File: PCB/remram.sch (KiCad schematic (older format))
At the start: 0 parts

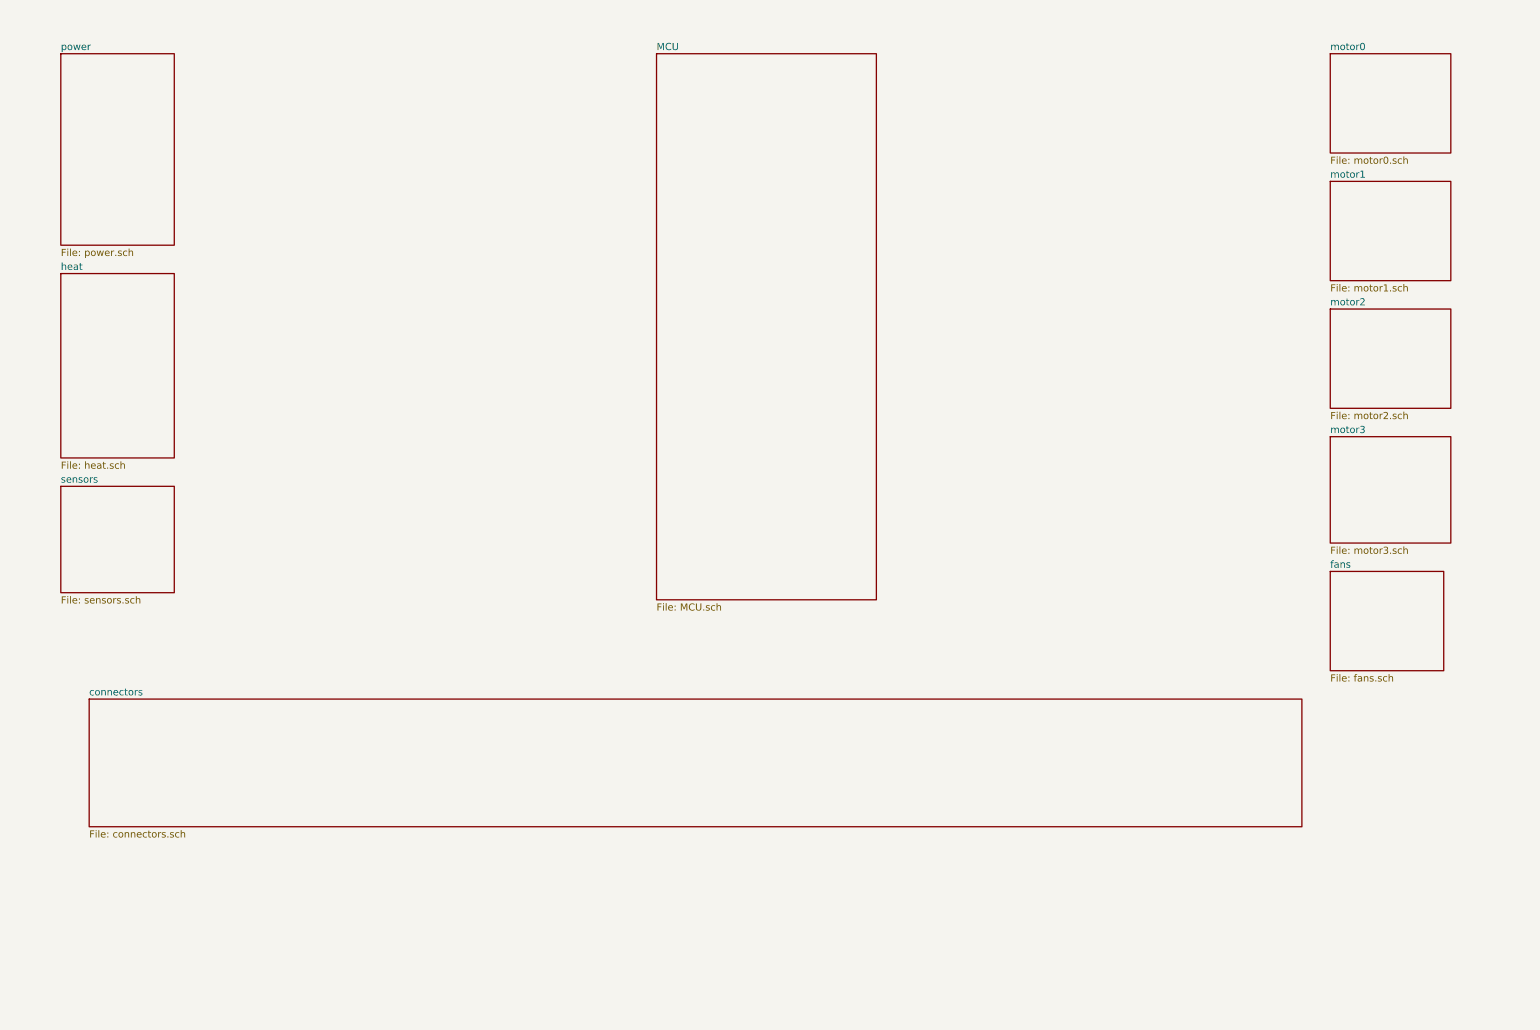
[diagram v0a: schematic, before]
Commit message: Changed PCB.
- Added MOSFET, connectors sheet
- Changed MCU and power sheet
- Reorganised sheets
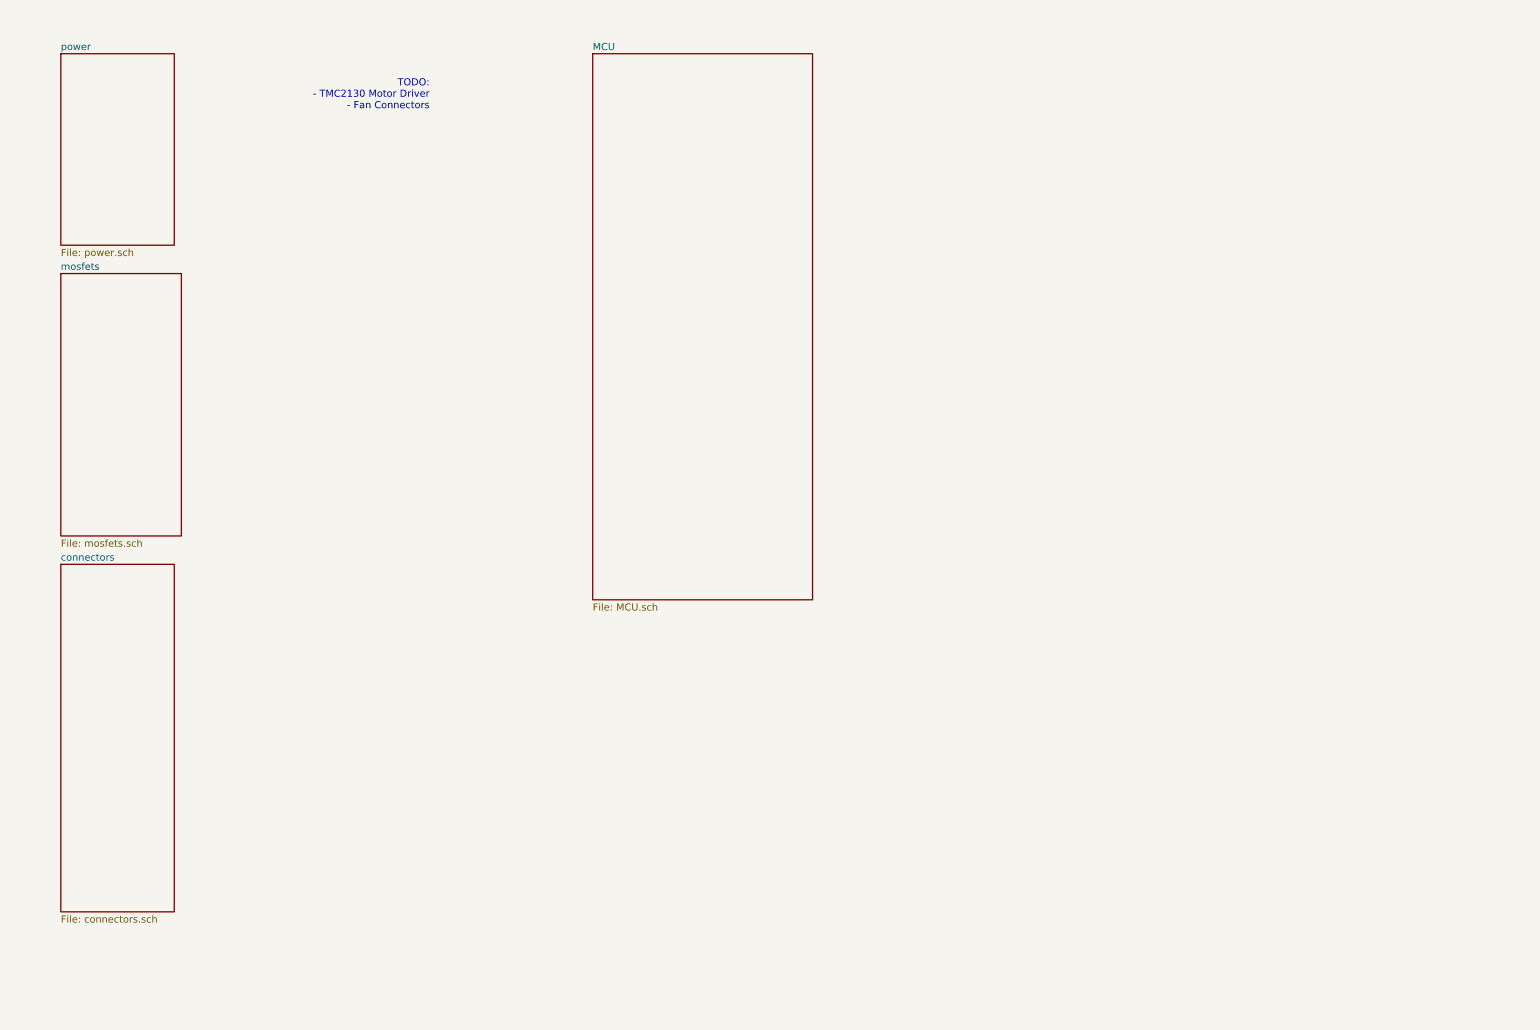
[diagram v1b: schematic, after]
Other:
- note added: "TODO: \n- TMC2130 Motor Driver\n- Fan Connectors"
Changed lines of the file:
@@
 $Descr A4 11693 8268
 encoding utf-8
-Sheet 1 11
-Title ""
+Sheet 1 5
+Title "Overview"
 Date ""
 Rev ""
@@
 $EndDescr
 $Sheet
-S 1050 5400 8550 900
-U 5AD05771
-F0 "connectors" 50
-F1 "connectors.sch" 50
-$EndSheet
-$Sheet
-S 9800 4500 800  700
-U 5AD055AC
-F0 "fans" 50
-F1 "fans.sch" 50
-$EndSheet
-$Sheet
-S 850  2400 800  1300
-U 5AD0552D
-F0 "heat" 50
-F1 "heat.sch" 50
-$EndSheet
-$Sheet
-S 5050 850  1550 3850
+S 4600 850  1550 3850
 U 5AD054EE
 F0 "MCU" 50
 F1 "MCU.sch" 50
-$EndSheet
-$Sheet
-S 9800 850  850  700
-U 5AD05561
-F0 "motor0" 50
-F1 "motor0.sch" 50
-$EndSheet
-$Sheet
-S 9800 1750 850  700
-U 5AD05578
-F0 "motor1" 50
-F1 "motor1.sch" 50
-$EndSheet
-$Sheet
-S 9800 2650 850  700
-U 5AD05586
-F0 "motor2" 50
-F1 "motor2.sch" 50
-$EndSheet
-$Sheet
-S 9800 3550 850  750
-U 5AD05626
-F0 "motor3" 50
-F1 "motor3.sch" 50
 $EndSheet
 $Sheet
@@
 $EndSheet
 $Sheet
-S 850  3900 800  750
-U 5AD05597
-F0 "sensors" 50
-F1 "sensors.sch" 50
+S 850  4450 800  2450
+U 5AF74780
+F0 "connectors" 50
+F1 "connectors.sch" 50
 $EndSheet
+$Sheet
+S 850  2400 850  1850
+U 5AF74A0B
+F0 "mosfets" 50
+F1 "mosfets.sch" 50
+$EndSheet
+Text Notes 3450 1250 2    50   ~ 0
+TODO: \n- TMC2130 Motor Driver\n- Fan Connectors
 $EndSCHEMATC

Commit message: Finished first draft of the schematics.
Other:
- note removed: "TODO: \n- TMC2130 Motor Driver\n- Fan Connectors"

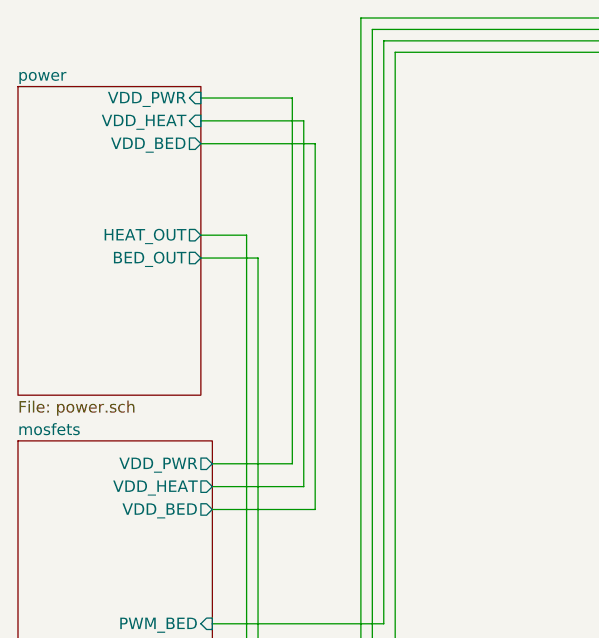
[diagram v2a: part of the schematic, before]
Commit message: Saving work in progress.
Every component now has a 3D mode.
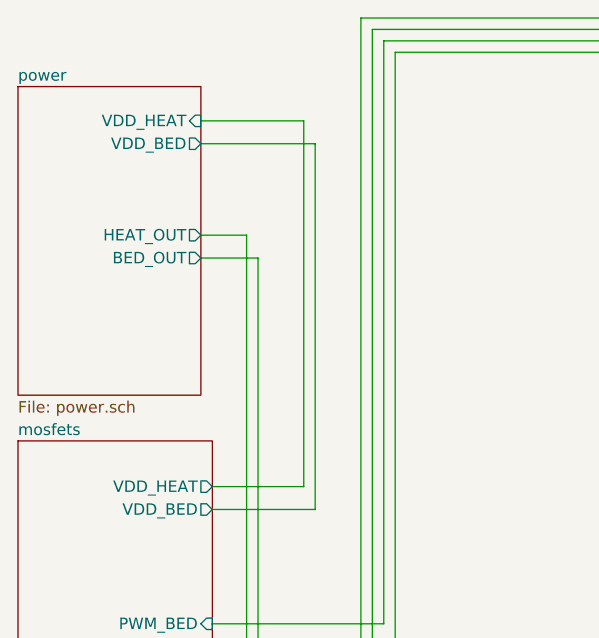
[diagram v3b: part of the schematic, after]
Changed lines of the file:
@@
 F4 "VDD_HEAT" I R 1650 1000 50
 F5 "HEAT_OUT" O R 1650 1500 50
-F6 "VDD_PWR" I R 1650 900 50
 $EndSheet
 $Sheet
@@
 F8 "PWM_FAN1" I R 1700 3400 50
 F9 "FAN1_OUT" O R 1700 4050 50
-F10 "VDD_PWR" O R 1700 2500 50
-F11 "FAN2_OUT" O R 1700 4150 50
-F12 "PWM_FAN2" I R 1700 3500 50
+F10 "FAN2_OUT" O R 1700 4150 50
+F11 "PWM_FAN2" I R 1700 3500 50
 $EndSheet
 $Sheet
@@
 $EndSheet
 Wire Wire Line
-	1650 900  2050 900
-Wire Wire Line
-	2050 900  2050 2500
-Wire Wire Line
-	2050 2500 1700 2500
-Wire Wire Line
 	1650 1000 2100 1000

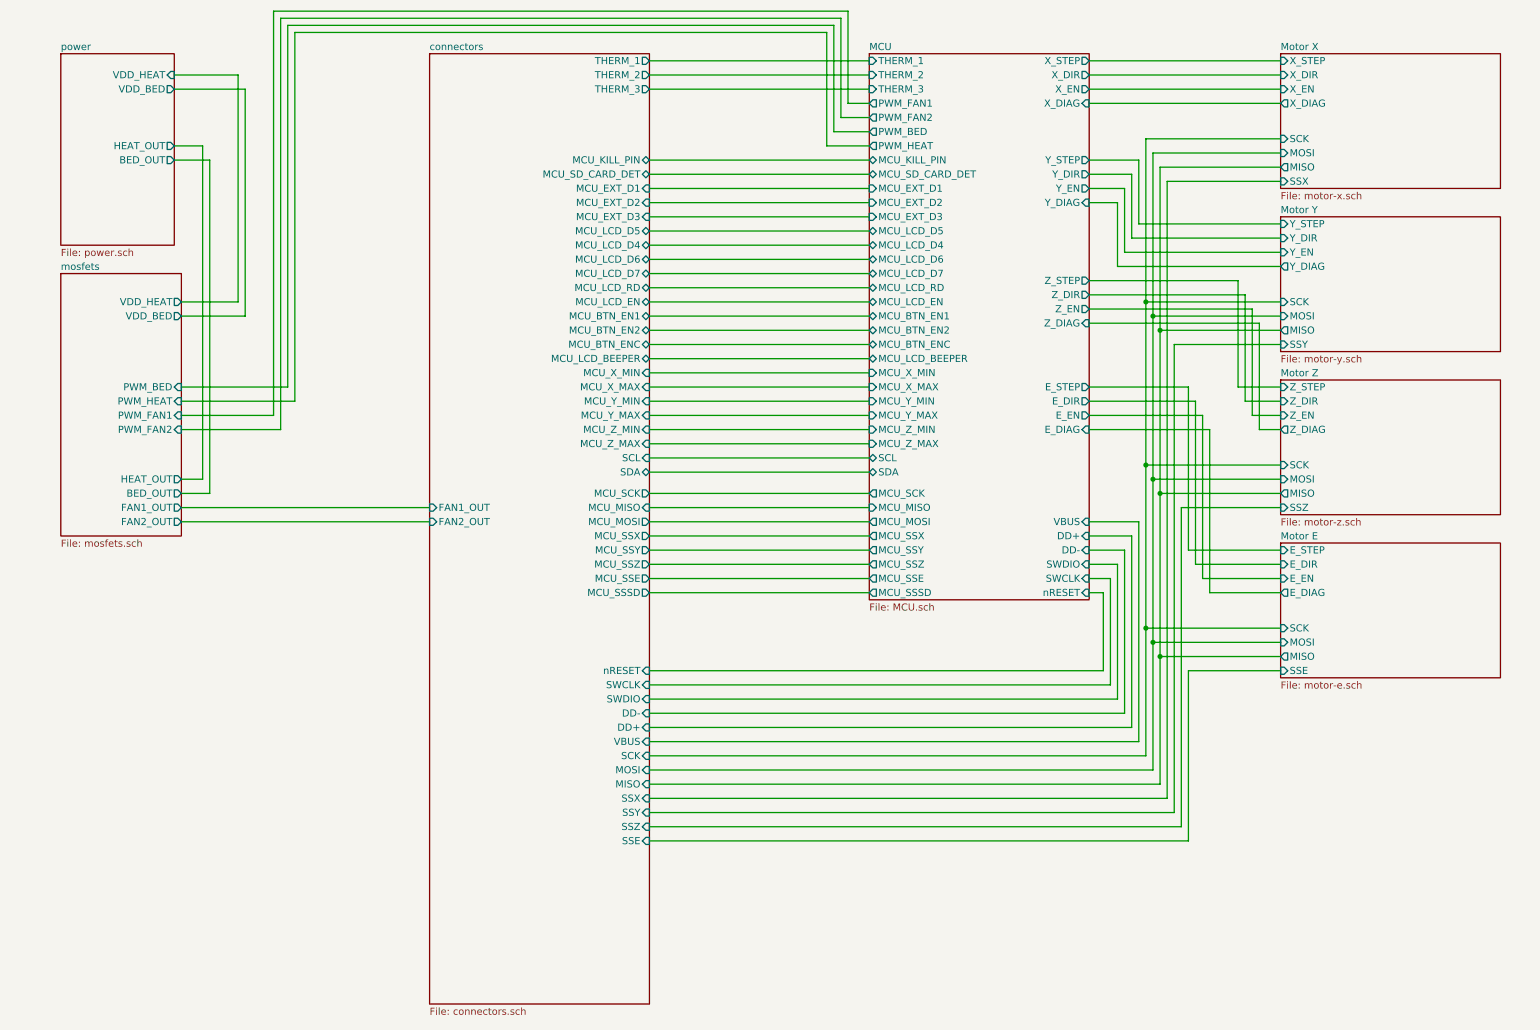
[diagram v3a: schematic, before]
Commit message: Removed logic level converter. Changed LDO.
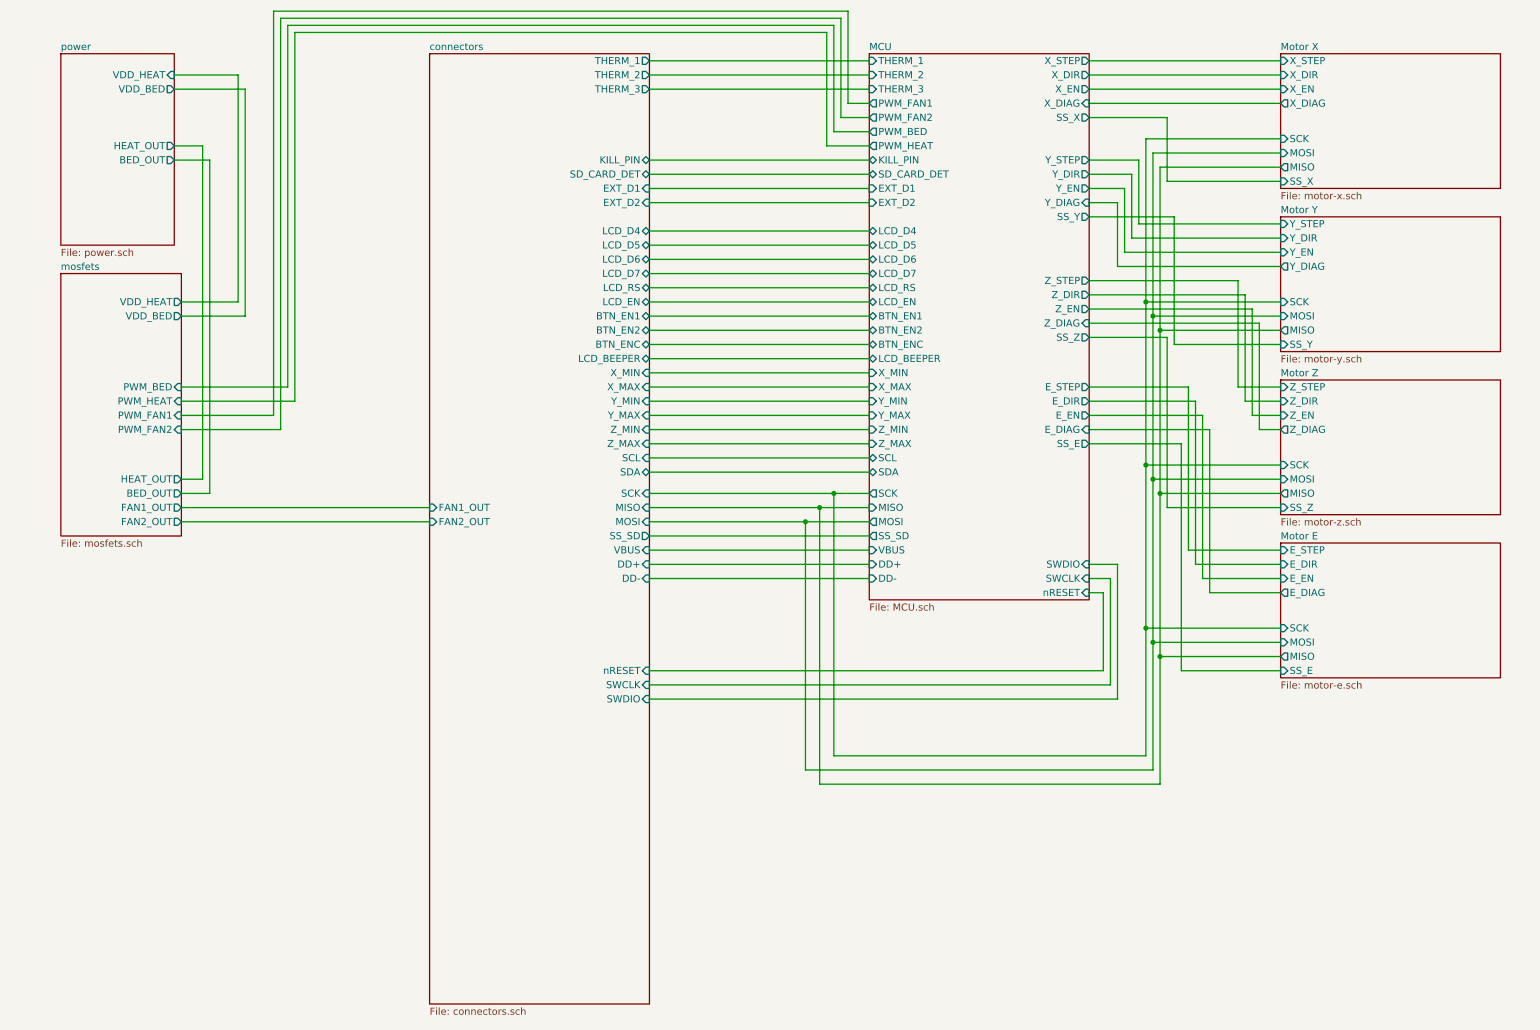
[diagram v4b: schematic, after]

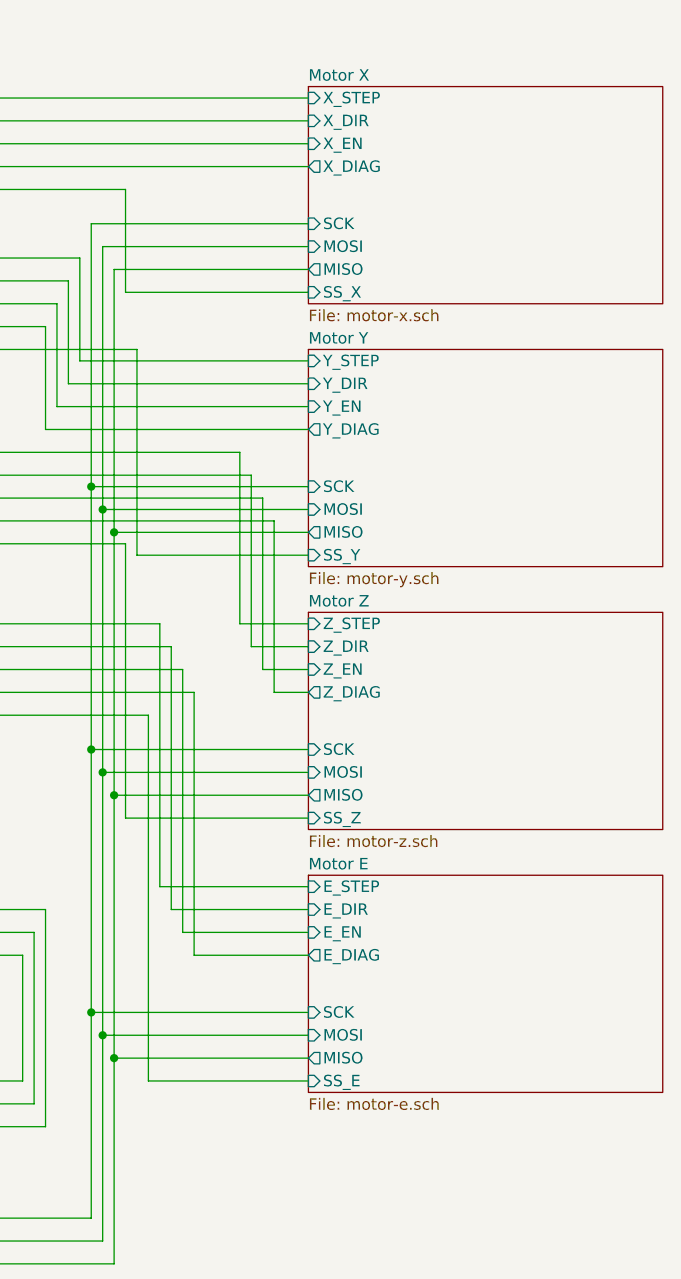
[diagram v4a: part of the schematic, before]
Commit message: Finished TMC2130 placement.
Motor sheets is now instanced. That way I simply could use
a KiCad plugin to duplicate the layout in Pcbnew.
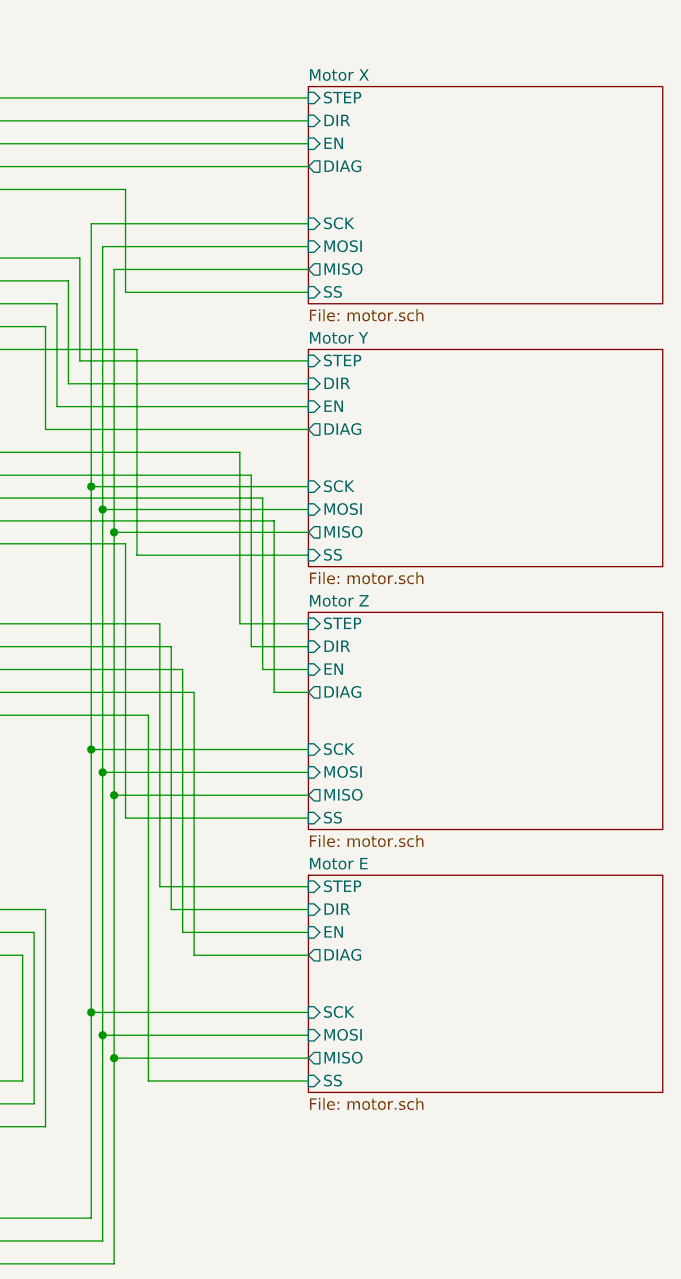
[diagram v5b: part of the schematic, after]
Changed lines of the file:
@@
 U 5B03041B
 F0 "Motor X" 50
-F1 "motor-x.sch" 50
-F2 "X_STEP" I L 9450 900 50
-F3 "X_DIR" I L 9450 1000 50
-F4 "X_EN" I L 9450 1100 50
-F5 "SCK" I L 9450 1450 50
-F6 "MOSI" I L 9450 1550 50
-F7 "MISO" O L 9450 1650 50
-F8 "X_DIAG" O L 9450 1200 50
-F9 "SS_X" I L 9450 1750 50
-$EndSheet
-$Sheet
-S 9450 2000 1550 950
-U 5B01ACF1
-F0 "Motor Y" 50
-F1 "motor-y.sch" 50
-F2 "Y_STEP" I L 9450 2050 50
-F3 "Y_DIR" I L 9450 2150 50
-F4 "Y_EN" I L 9450 2250 50
-F5 "SCK" I L 9450 2600 50
-F6 "MOSI" I L 9450 2700 50
-F7 "MISO" O L 9450 2800 50
-F8 "Y_DIAG" O L 9450 2350 50
-F9 "SS_Y" I L 9450 2900 50
-$EndSheet
-$Sheet
-S 9450 3150 1550 950
-U 5B01E3E9
-F0 "Motor Z" 50
-F1 "motor-z.sch" 50
-F2 "Z_STEP" I L 9450 3200 50
-F3 "Z_DIR" I L 9450 3300 50
-F4 "Z_EN" I L 9450 3400 50
-F5 "SCK" I L 9450 3750 50
-F6 "MOSI" I L 9450 3850 50
-F7 "MISO" O L 9450 3950 50
-F8 "Z_DIAG" O L 9450 3500 50
-F9 "SS_Z" I L 9450 4050 50
-$EndSheet
-$Sheet
-S 9450 4300 1550 950
-U 5B02189F
-F0 "Motor E" 50
-F1 "motor-e.sch" 50
-F2 "E_STEP" I L 9450 4350 50
-F3 "E_DIR" I L 9450 4450 50
-F4 "E_EN" I L 9450 4550 50
-F5 "SCK" I L 9450 4900 50
-F6 "MOSI" I L 9450 5000 50
-F7 "MISO" O L 9450 5100 50
-F8 "E_DIAG" O L 9450 4650 50
-F9 "SS_E" I L 9450 5200 50
+F1 "motor.sch" 50
+F2 "SCK" I L 9450 1450 50
+F3 "MOSI" I L 9450 1550 50
+F4 "MISO" O L 9450 1650 50
+F5 "STEP" I L 9450 900 50
+F6 "DIR" I L 9450 1000 50
+F7 "EN" I L 9450 1100 50
+F8 "SS" I L 9450 1750 50
+F9 "DIAG" O L 9450 1200 50
 $EndSheet
 Wire Wire Line
@@
 F38 "EXT_D2" I R 5000 1900 50
 $EndSheet
+$Sheet
+S 9450 2000 1550 950
+U 5AFC22B0
+F0 "Motor Y" 50
+F1 "motor.sch" 50
+F2 "SCK" I L 9450 2600 50
+F3 "MOSI" I L 9450 2700 50
+F4 "MISO" O L 9450 2800 50
+F5 "STEP" I L 9450 2050 50
+F6 "DIR" I L 9450 2150 50
+F7 "EN" I L 9450 2250 50
+F8 "SS" I L 9450 2900 50
+F9 "DIAG" O L 9450 2350 50
+$EndSheet
+$Sheet
+S 9450 3150 1550 950
+U 5AFC9D86
+F0 "Motor Z" 50
+F1 "motor.sch" 50
+F2 "SCK" I L 9450 3750 50
+F3 "MOSI" I L 9450 3850 50
+F4 "MISO" O L 9450 3950 50
+F5 "STEP" I L 9450 3200 50
+F6 "DIR" I L 9450 3300 50
+F7 "EN" I L 9450 3400 50
+F8 "SS" I L 9450 4050 50
+F9 "DIAG" O L 9450 3500 50
+$EndSheet
+$Sheet
+S 9450 4300 1550 950
+U 5AFD185C
+F0 "Motor E" 50
+F1 "motor.sch" 50
+F2 "SCK" I L 9450 4900 50
+F3 "MOSI" I L 9450 5000 50
+F4 "MISO" O L 9450 5100 50
+F5 "STEP" I L 9450 4350 50
+F6 "DIR" I L 9450 4450 50
+F7 "EN" I L 9450 4550 50
+F8 "SS" I L 9450 5200 50
+F9 "DIAG" O L 9450 4650 50
+$EndSheet
 $EndSCHEMATC
